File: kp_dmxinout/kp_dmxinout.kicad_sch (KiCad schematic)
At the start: 21 parts, among them J1 NC3MAAH, J2 NC3FAAH, J3 Conn_01x04, U1 SN75176AD, U2 6N137, U3 6N137, U4 SN75176AD

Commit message: dmxinout: do board
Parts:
- added C7, C8: 1u, Capacitor_SMD:C_1206_3216Metric, symbol Device:C_Small
- C1, C2: footprint (none) -> Capacitor_SMD:C_1206_3216Metric
- C3, C4, C5, C6: footprint (none) -> Capacitor_SMD:C_0402_1005Metric
- J3: footprint Connector_JST:JST_XH_B4B-XH-A_1x04_P2.50mm_Vertical -> Connector_IDC:IDC-Header_2x03_P2.54mm_Vertical; symbol Connector_Generic:Conn_01x04 -> Connector_Generic:Conn_01x06
- R1, R2, R3, R4, R5, R6, R7: footprint (none) -> Resistor_SMD:R_0603_1608Metric
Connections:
- net GND: now also C7.1, C8.1
- net IN_DATATTL: no longer R5.2, U3.6 (VO), U4.4 (D)
- net 6n137_out_c: now reaches R3.1, U3.3 (C)
- net 6n137_in_c: now reaches R1.2, U2.3 (C)
- removed net Earth: J1.1, J1.G, J2.1
- net IN_DATAMINUS renamed IN_DATA-
- net IN_DATAPLUS renamed IN_DATA+
- net OUT_DATAMINUS renamed OUT_DATA-
- net OUT_DATAPLUS renamed OUT_DATA+
- new net IN_SHIELD: C7.2, J1.1
- new net OUT_DATATTL: R5.2, U3.6 (VO), U4.4 (D)
- new net OUT_SHIELD: C8.2, J2.1
- no-connect marks 4 -> 5
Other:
- moved on the sheet: R1, R3, R4

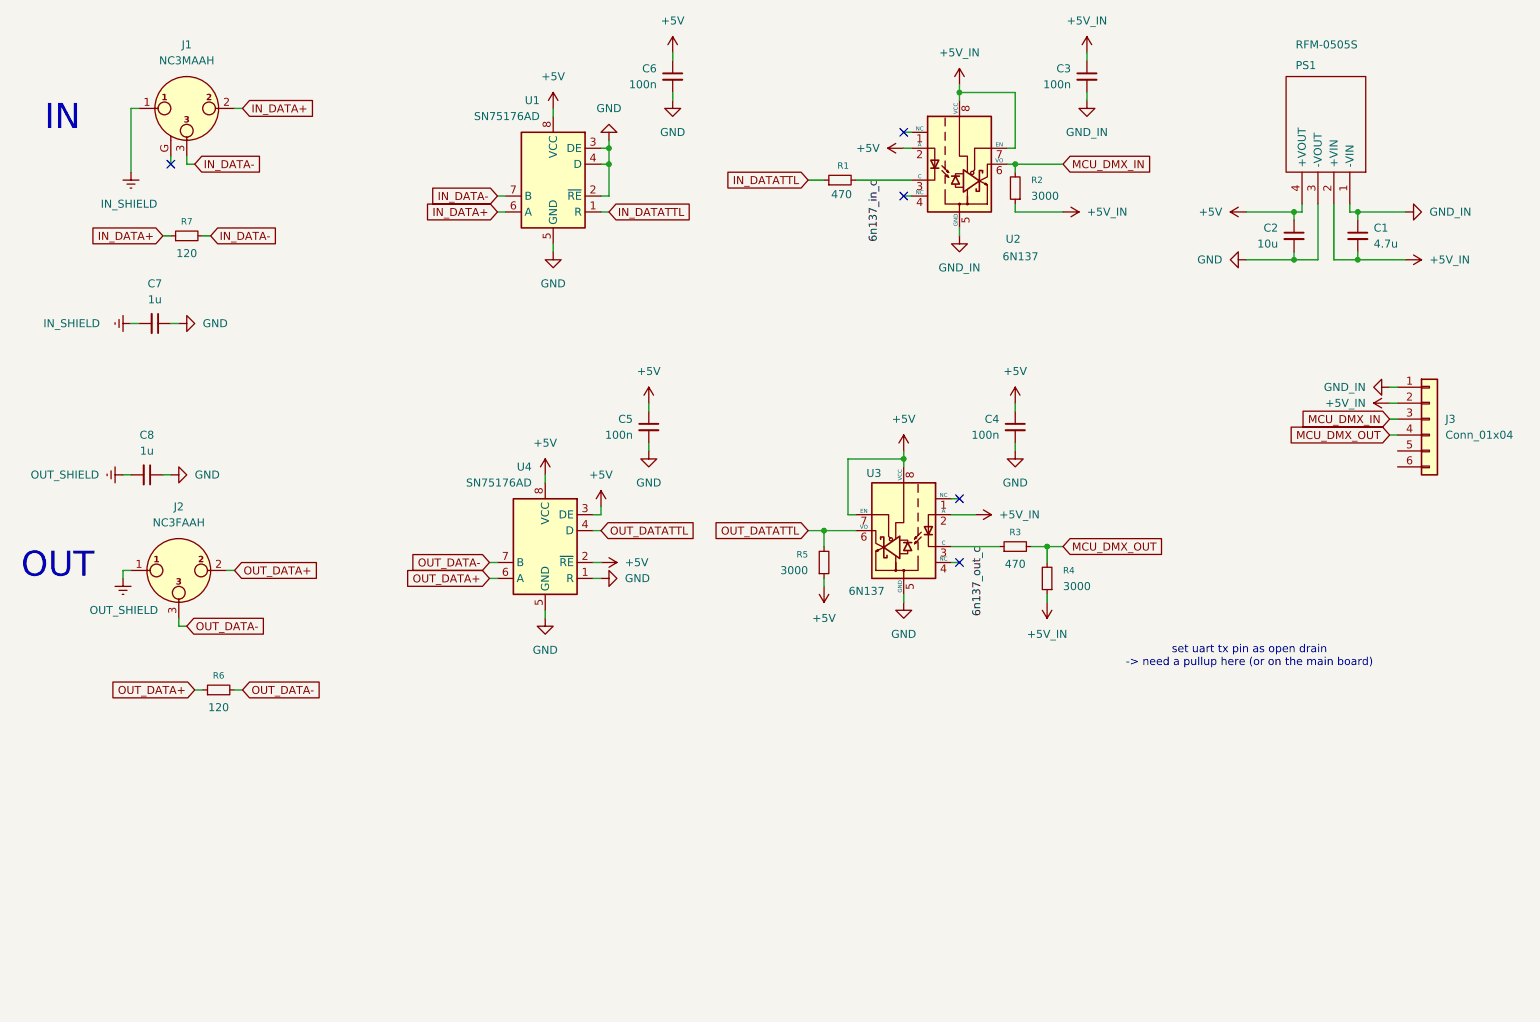
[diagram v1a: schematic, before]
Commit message: dmx: disconnect shield & gnd
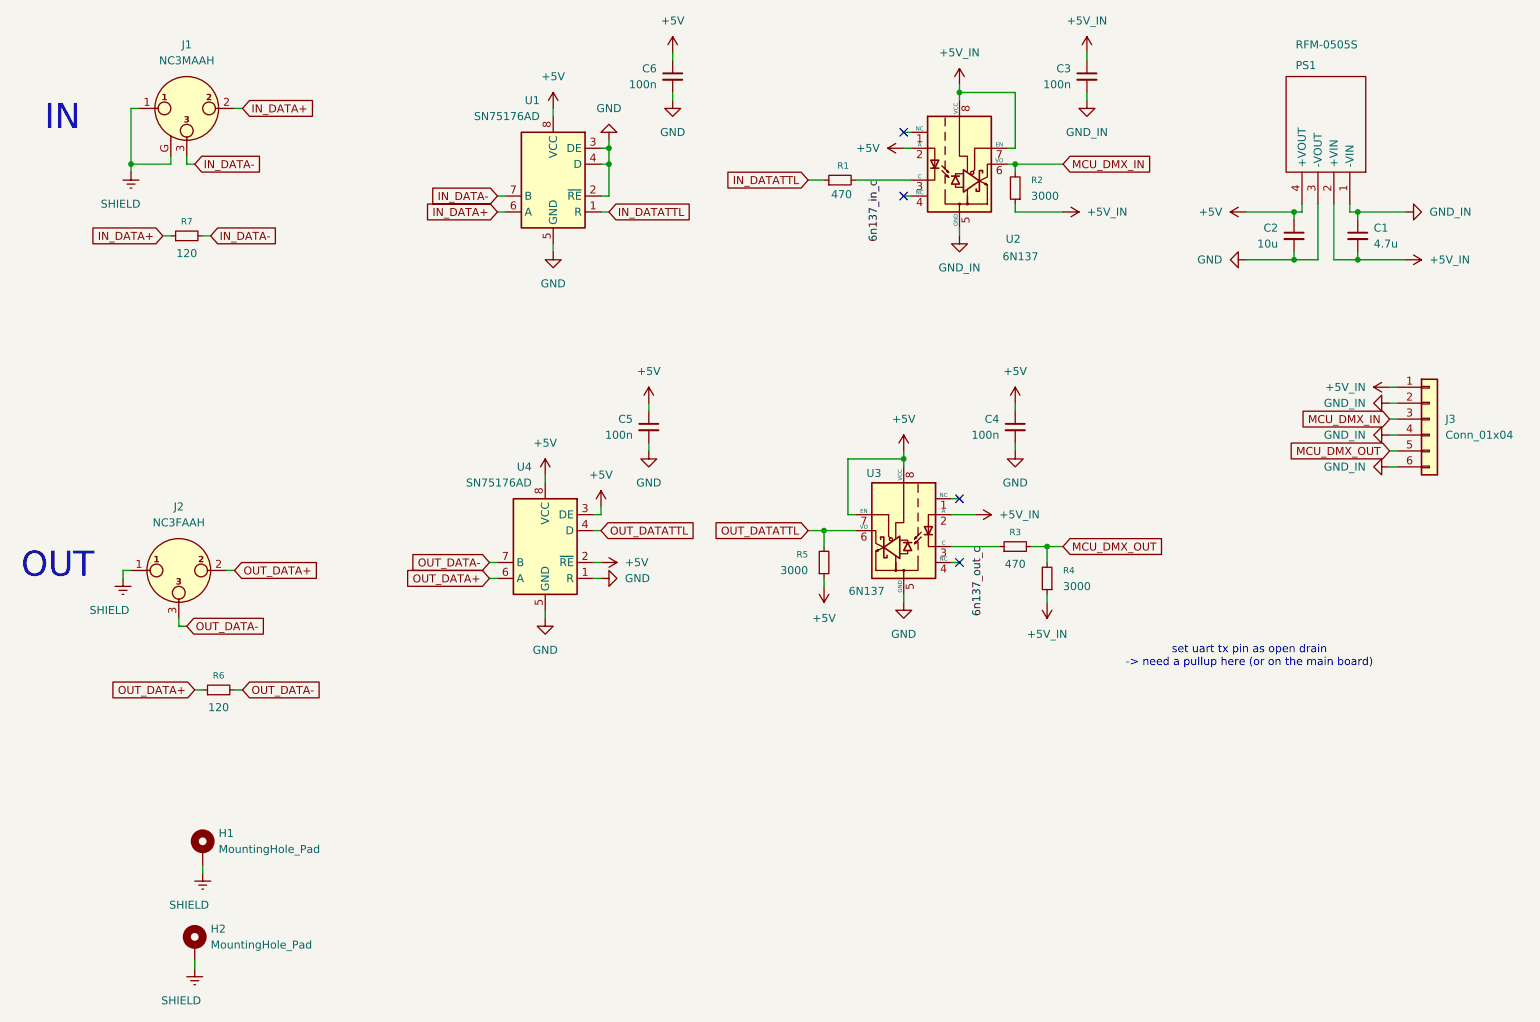
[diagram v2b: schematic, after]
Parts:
- removed C7, C8: 1u, Capacitor_SMD:C_1206_3216Metric, symbol Device:C_Small
- added H1, H2: MountingHole_Pad, MountingHole:MountingHole_3.2mm_M3_Pad_Via, symbol Mechanical:MountingHole_Pad
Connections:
- net IN_SHIELD is gone; now on net SHIELD: J1.1
- net OUT_SHIELD is gone; now on net SHIELD: J2.1
- net +5V_IN: now also J3.1 (Pin_1); no longer J3.2 (Pin_2)
- net GND_IN: now also J3.2 (Pin_2), J3.4 (Pin_4), J3.6 (Pin_6); no longer J3.1 (Pin_1)
- net MCU_DMX_OUT: now also J3.5 (Pin_5); no longer J3.4 (Pin_4)
- net SHIELD: now reaches J1.G
- net SHIELD: now also H1.1, H2.1
- no-connect marks 5 -> 4

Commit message: main board : start doing sig gnd gnd sigpow
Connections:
- net +5V_IN: now also J3.2 (Pin_2); no longer J3.1 (Pin_1)
- net GND_IN: now also J3.1 (Pin_1), J3.3 (Pin_3), J3.5 (Pin_5); no longer J3.2 (Pin_2), J3.4 (Pin_4), J3.6 (Pin_6)
- net MCU_DMX_IN: now also J3.4 (Pin_4); no longer J3.3 (Pin_3)
- net MCU_DMX_OUT: now also J3.6 (Pin_6); no longer J3.5 (Pin_5)
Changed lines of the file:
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@@
 	(global_label "MCU_DMX_IN"
 		(shape input)
-		(at 229.87 80.01 180)
+		(at 229.87 82.55 180)
 		(fields_autoplaced yes)
 		(effects
@@
 		)
 		(property "Intersheetrefs" "${INTERSHEET_REFS}"
-			(at 215.0315 80.01 0)
+			(at 215.0315 82.55 0)
 			(hide yes)
 			(show_name no)
@@
 	(global_label "MCU_DMX_OUT"
 		(shape input)
-		(at 229.87 85.09 180)
+		(at 229.87 87.63 180)
 		(fields_autoplaced yes)
 		(effects
@@
 		)
 		(property "Intersheetrefs" "${INTERSHEET_REFS}"
-			(at 213.3382 85.09 0)
+			(at 213.3382 87.63 0)
 			(hide yes)
 			(show_name no)
@@
 	(symbol
 		(lib_id "power:GND")
-		(at 229.87 87.63 270)
+		(at 229.87 85.09 270)
 		(mirror x)
 		(unit 1)
@@
 		(dnp no)
 		(property "Reference" "#PWR040"
-			(at 223.52 87.63 0)
+			(at 223.52 85.09 0)
 			(hide yes)
 			(show_name no)
@@
 		)
 		(property "Value" "GND_IN"
-			(at 226.06 87.6301 90)
+			(at 226.06 85.0901 90)
 			(show_name no)
 			(do_not_autoplace no)
@@
 		)
 		(property "Footprint" ""
-			(at 229.87 87.63 0)
+			(at 229.87 85.09 0)
 			(hide yes)
 			(show_name no)
@@
 		)
 		(property "Datasheet" ""
-			(at 229.87 87.63 0)
+			(at 229.87 85.09 0)
 			(hide yes)
 			(show_name no)
@@
 		)
 		(property "Description" "Power symbol creates a global label with name \"GND\" , ground"
-			(at 229.87 87.63 0)
+			(at 229.87 85.09 0)
 			(hide yes)
 			(show_name no)
@@
 	(symbol
 		(lib_id "power:GND")
-		(at 229.87 82.55 270)
+		(at 229.87 80.01 270)
 		(mirror x)
 		(unit 1)
@@
 		(dnp no)
 		(property "Reference" "#PWR039"
-			(at 223.52 82.55 0)
+			(at 223.52 80.01 0)
 			(hide yes)
 			(show_name no)
@@
 		)
 		(property "Value" "GND_IN"
-			(at 226.06 82.5501 90)
+			(at 226.06 80.0101 90)
 			(show_name no)
 			(do_not_autoplace no)
@@
 		)
 		(property "Footprint" ""
-			(at 229.87 82.55 0)
+			(at 229.87 80.01 0)
 			(hide yes)
 			(show_name no)
@@
 		)
 		(property "Datasheet" ""
-			(at 229.87 82.55 0)
+			(at 229.87 80.01 0)
 			(hide yes)
 			(show_name no)
@@
 		)
 		(property "Description" "Power symbol creates a global label with name \"GND\" , ground"
-			(at 229.87 82.55 0)
+			(at 229.87 80.01 0)
 			(hide yes)
 			(show_name no)
@@
 	(symbol
 		(lib_id "power:+5V")
-		(at 229.87 74.93 90)
+		(at 229.87 77.47 90)
 		(unit 1)
 		(body_style 1)
@@
 		(fields_autoplaced yes)
 		(property "Reference" "#PWR015"
-			(at 233.68 74.93 0)
+			(at 233.68 77.47 0)
 			(hide yes)
 			(show_name no)
@@
 		)
 		(property "Value" "+5V_IN"
-			(at 226.06 74.9299 90)
+			(at 226.06 77.4699 90)
 			(show_name no)
 			(do_not_autoplace no)
@@
 		)
 		(property "Footprint" ""
-			(at 229.87 74.93 0)
+			(at 229.87 77.47 0)
 			(hide yes)
 			(show_name no)
@@
 		)
 		(property "Datasheet" ""
-			(at 229.87 74.93 0)
+			(at 229.87 77.47 0)
 			(hide yes)
 			(show_name no)
@@
 		)
 		(property "Description" "Power symbol creates a global label with name \"+5V\""
-			(at 229.87 74.93 0)
+			(at 229.87 77.47 0)
 			(hide yes)
 			(show_name no)
@@
 	(symbol
 		(lib_id "power:GND")
-		(at 229.87 77.47 270)
+		(at 229.87 74.93 270)
 		(mirror x)
 		(unit 1)
@@
 		(dnp no)
 		(property "Reference" "#PWR014"
-			(at 223.52 77.47 0)
+			(at 223.52 74.93 0)
 			(hide yes)
 			(show_name no)
@@
 		)
 		(property "Value" "GND_IN"
-			(at 226.06 77.4701 90)
+			(at 226.06 74.9301 90)
 			(show_name no)
 			(do_not_autoplace no)
@@
 		)
 		(property "Footprint" ""
-			(at 229.87 77.47 0)
+			(at 229.87 74.93 0)
 			(hide yes)
 			(show_name no)
@@
 		)
 		(property "Datasheet" ""
-			(at 229.87 77.47 0)
+			(at 229.87 74.93 0)
 			(hide yes)
 			(show_name no)
@@
 		)
 		(property "Description" "Power symbol creates a global label with name \"GND\" , ground"
-			(at 229.87 77.47 0)
+			(at 229.87 74.93 0)
 			(hide yes)
 			(show_name no)

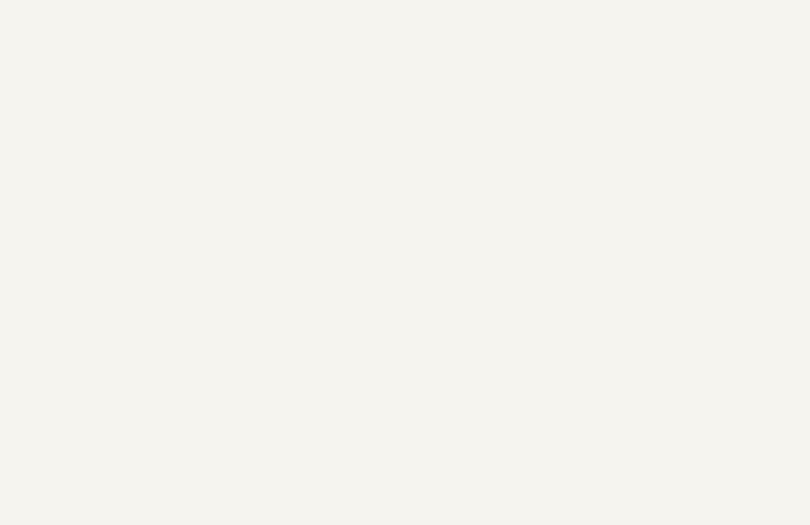
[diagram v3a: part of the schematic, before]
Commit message: add pwr leds
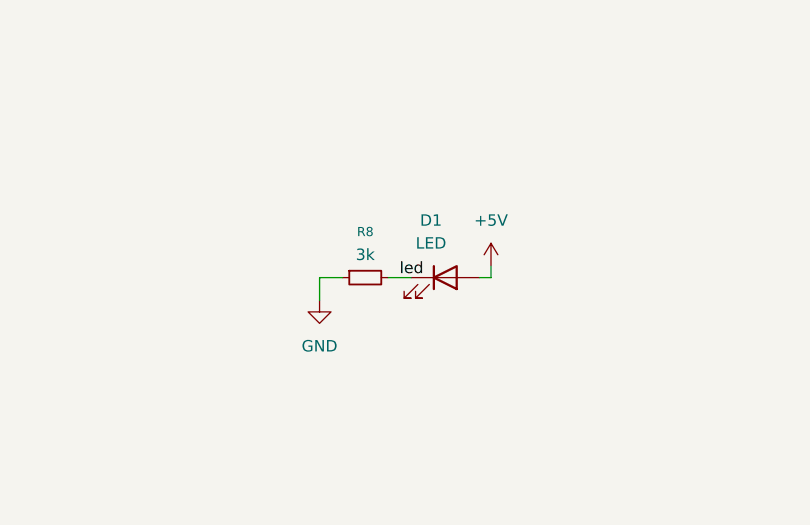
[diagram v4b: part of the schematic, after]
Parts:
- added D1: LED, LED_SMD:LED_0805_2012Metric, symbol Device:LED
- added R8: 3k, Resistor_SMD:R_0805_2012Metric, symbol Device:R_Small
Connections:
- net +5V: now also D1.2 (A)
- net GND: now also R8.1
- new net led: D1.1 (K), R8.2

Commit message: ready 4 prod
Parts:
- C1: LCSC (none) -> C51205
- C2: LCSC (none) -> C13585
- C3, C4, C5, C6: LCSC (none) -> C1525
- D1: LCSC https://www.lcsc.com/product-detail/C965812.html -> C965812
- J1: LCSC (none) -> C368463
- J2: LCSC (none) -> C368521
- J3: LCSC (none) -> C11214
- PS1: LCSC (none) -> C22371855
- R1, R3: LCSC (none) -> C844786
- R2, R4, R5: value 3000 -> 3k; footprint Resistor_SMD:R_0603_1608Metric -> Resistor_SMD:R_0805_2012Metric; LCSC (none) -> C126350
- R6, R7: LCSC (none) -> C844736
- R8: LCSC (none) -> C126350
- U1, U4: LCSC (none) -> C468242
- U2, U3: LCSC (none) -> C142297
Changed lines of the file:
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@@
 			)
 		)
-		(property "LCSC" ""
+		(property "LCSC" "C368463"
 			(at 38.1 30.48 0)
 			(hide yes)
@@
 			)
 		)
-		(property "LCSC" ""
+		(property "LCSC" "C844736"
 			(at 38.1 50.8 90)
 			(hide yes)
@@
 			)
 		)
-		(property "LCSC" ""
+		(property "LCSC" "C468242"
 			(at 95.25 100.33 0)
 			(hide yes)
@@
 			)
 		)
-		(property "LCSC" ""
+		(property "LCSC" "C142297"
 			(at 152.4 97.79 0)
 			(hide yes)
@@
 			)
 		)
-		(property "LCSC" ""
+		(property "LCSC" "C22371855"
 			(at 223.52 45.72 90)
 			(hide yes)
@@
 			)
 		)
-		(property "Value" "3000"
+		(property "Value" "3k"
 			(at 137.16 104.1399 0)
 			(show_name no)
@@
 			)
 		)
-		(property "Footprint" "Resistor_SMD:R_0603_1608Metric"
+		(property "Footprint" "Resistor_SMD:R_0805_2012Metric"
 			(at 139.7 102.87 0)
 			(hide yes)
@@
 			)
 		)
-		(property "LCSC" ""
+		(property "LCSC" "C126350"
 			(at 139.7 102.87 0)
 			(hide yes)
@@
 			)
 		)
-		(property "Value" "3000"
+		(property "Value" "3k"
 			(at 177.8 106.6799 0)
 			(show_name no)
@@
 			)
 		)
-		(property "Footprint" "Resistor_SMD:R_0603_1608Metric"
+		(property "Footprint" "Resistor_SMD:R_0805_2012Metric"
 			(at 175.26 105.41 0)
 			(hide yes)
@@
 			)
 		)
-		(property "LCSC" ""
+		(property "LCSC" "C126350"
 			(at 175.26 105.41 0)
 			(hide yes)
@@
 			)
 		)
-		(property "LCSC" ""
+		(property "LCSC" "C468242"
 			(at 96.52 41.91 0)
 			(hide yes)
@@
 			)
 		)
-		(property "LCSC" ""
+		(property "LCSC" "C844786"
 			(at 142.24 41.91 90)
 			(hide yes)
@@
 			)
 		)
-		(property "LCSC" "https://www.lcsc.com/product-detail/C965812.html"
+		(property "LCSC" "C965812"
 			(at 109.22 148.59 0)
 			(hide yes)
@@
 			)
 		)
-		(property "LCSC" ""
+		(property "LCSC" "C126350"
 			(at 100.33 148.59 90)
 			(hide yes)
@@
 			)
 		)
-		(property "LCSC" ""
+		(property "LCSC" "C11214"
 			(at 236.22 80.01 0)
 			(hide yes)
@@
 			)
 		)
-		(property "Value" "3000"
+		(property "Value" "3k"
 			(at 172.72 44.4499 0)
 			(show_name no)
@@
 			)
 		)
-		(property "Footprint" "Resistor_SMD:R_0603_1608Metric"
+		(property "Footprint" "Resistor_SMD:R_0805_2012Metric"
 			(at 170.18 43.18 0)
 			(hide yes)
@@
 			)
 		)
-		(property "LCSC" ""
+		(property "LCSC" "C126350"
 			(at 170.18 43.18 0)
 			(hide yes)
@@
 			)
 		)
-		(property "LCSC" ""
+		(property "LCSC" "C13585"
 			(at 214.63 50.8 0)
 			(hide yes)
@@
 			)
 		)
-		(property "LCSC" ""
+		(property "LCSC" "C1525"
 			(at 181.61 25.4 0)
 			(hide yes)
@@
 			)
 		)
-		(property "LCSC" ""
+		(property "LCSC" "C51205"
 			(at 224.79 50.8 0)
 			(hide yes)
@@
 			)
 		)
-		(property "LCSC" ""
+		(property "LCSC" "C1525"
 			(at 115.57 25.4 0)
 			(hide yes)
@@
 			)
 		)
-		(property "LCSC" ""
+		(property "LCSC" "C1525"
 			(at 170.18 81.28 0)
 			(hide yes)
@@
 			)
 		)
-		(property "LCSC" ""
+		(property "LCSC" "C844786"
 			(at 170.18 100.33 90)
 			(hide yes)
@@
 			)
 		)
-		(property "LCSC" ""
+		(property "LCSC" "C1525"
 			(at 111.76 81.28 0)
 			(hide yes)
@@
 			)
 		)
-		(property "LCSC" ""
+		(property "LCSC" "C844736"
 			(at 43.18 123.19 90)
 			(hide yes)
@@
 			)
 		)
-		(property "LCSC" ""
+		(property "LCSC" "C368521"
 			(at 36.83 104.14 0)
 			(hide yes)
@@
 			)
 		)
-		(property "LCSC" ""
+		(property "LCSC" "C142297"
 			(at 161.29 39.37 0)
 			(hide yes)
